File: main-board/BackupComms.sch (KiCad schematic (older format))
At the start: 0 parts

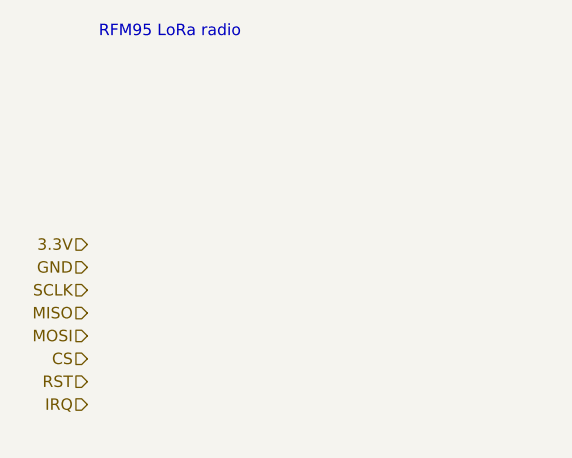
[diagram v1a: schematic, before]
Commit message: more subsheets
backup coms
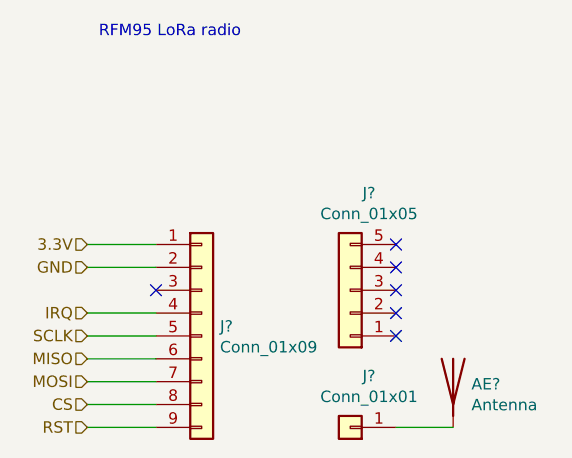
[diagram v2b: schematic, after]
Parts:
- added AE?: Antenna, symbol Device:Antenna
- added J?: Conn_01x09, symbol Connector_Generic:Conn_01x09
- added J?: Conn_01x05, symbol Connector_Generic:Conn_01x05
- added J?: Conn_01x01, symbol Connector_Generic:Conn_01x01
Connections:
- net 3.3V: now also J?.1 (Pin_1)
- net CS: now also J?.8 (Pin_8)
- net GND: now also J?.2 (Pin_2)
- net IRQ: now also J?.4 (Pin_4)
- net MISO: now also J?.6 (Pin_6)
- net MOSI: now also J?.7 (Pin_7)
- net RST: now also J?.9 (Pin_9)
- net SCLK: now also J?.5 (Pin_5)
- new net: AE?.1 (A), J?.1 (Pin_1)
- no-connect marks 0 -> 6
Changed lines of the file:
@@
 Text HLabel 2850 3050 0    50   Input ~ 0
 GND
-Text HLabel 2850 3150 0    50   Input ~ 0
+Text HLabel 2850 3350 0    50   Input ~ 0
 SCLK
+Text HLabel 2850 3450 0    50   Input ~ 0
+MISO
+Text HLabel 2850 3550 0    50   Input ~ 0
+MOSI
+Text HLabel 2850 3650 0    50   Input ~ 0
+CS
+Text HLabel 2850 3750 0    50   Input ~ 0
+RST
 Text HLabel 2850 3250 0    50   Input ~ 0
-MISO
-Text HLabel 2850 3350 0    50   Input ~ 0
-MOSI
-Text HLabel 2850 3450 0    50   Input ~ 0
-CS
-Text HLabel 2850 3550 0    50   Input ~ 0
-RST
-Text HLabel 2850 3650 0    50   Input ~ 0
 IRQ
 Text Notes 2900 2050 0    50   ~ 0
 RFM95 LoRa radio
+$Comp
+L Connector_Generic:Conn_01x09 J?
+U 1 1 60C632E9
+P 3350 3350
+F 0 "J?" H 3430 3392 50  0000 L CNN
+F 1 "Conn_01x09" H 3430 3301 50  0000 L CNN
+F 2 "" H 3350 3350 50  0001 C CNN
+F 3 "~" H 3350 3350 50  0001 C CNN
+	1    3350 3350
+	1    0    0    -1
+$EndComp
+NoConn ~ 3150 3150
+Wire Wire Line
+	2850 2950 3150 2950
+Wire Wire Line
+	3150 3050 2850 3050
+Wire Wire Line
+	2850 3250 3150 3250
+Wire Wire Line
+	3150 3350 2850 3350
+Wire Wire Line
+	2850 3450 3150 3450
+Wire Wire Line
+	3150 3550 2850 3550
+Wire Wire Line
+	2850 3650 3150 3650
+Wire Wire Line
+	3150 3750 2850 3750
+$Comp
+L Connector_Generic:Conn_01x05 J?
+U 1 1 60C655C7
+P 4000 3150
+F 0 "J?" H 3918 2725 50  0000 C CNN
+F 1 "Conn_01x05" H 3918 2816 50  0000 C CNN
+F 2 "" H 4000 3150 50  0001 C CNN
+F 3 "~" H 4000 3150 50  0001 C CNN
+	1    4000 3150
+	-1   0    0    1
+$EndComp
+NoConn ~ 4200 2950
+NoConn ~ 4200 3050
+NoConn ~ 4200 3150
+NoConn ~ 4200 3250
+NoConn ~ 4200 3350
+$Comp
+L Connector_Generic:Conn_01x01 J?
+U 1 1 60C66805
+P 4000 3750
+F 0 "J?" H 3918 3525 50  0000 C CNN
+F 1 "Conn_01x01" H 3918 3616 50  0000 C CNN
+F 2 "" H 4000 3750 50  0001 C CNN
+F 3 "~" H 4000 3750 50  0001 C CNN
+	1    4000 3750
+	-1   0    0    1
+$EndComp
+$Comp
+L Device:Antenna AE?
+U 1 1 60C67335
+P 4450 3550
+F 0 "AE?" H 4530 3539 50  0000 L CNN
+F 1 "Antenna" H 4530 3448 50  0000 L CNN
+F 2 "" H 4450 3550 50  0001 C CNN
+F 3 "~" H 4450 3550 50  0001 C CNN
+	1    4450 3550
+	1    0    0    -1
+$EndComp
+Wire Wire Line
+	4450 3750 4200 3750
 $EndSCHEMATC
